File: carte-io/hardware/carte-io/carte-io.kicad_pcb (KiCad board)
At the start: 2 copper layers, 100 x 80 mm, 4 parts, among them J1 USB_C_Receptacle_USB2.0_14P, J2 Conn_01x02, U1 STM32U545VETx, U2 FT231XQ

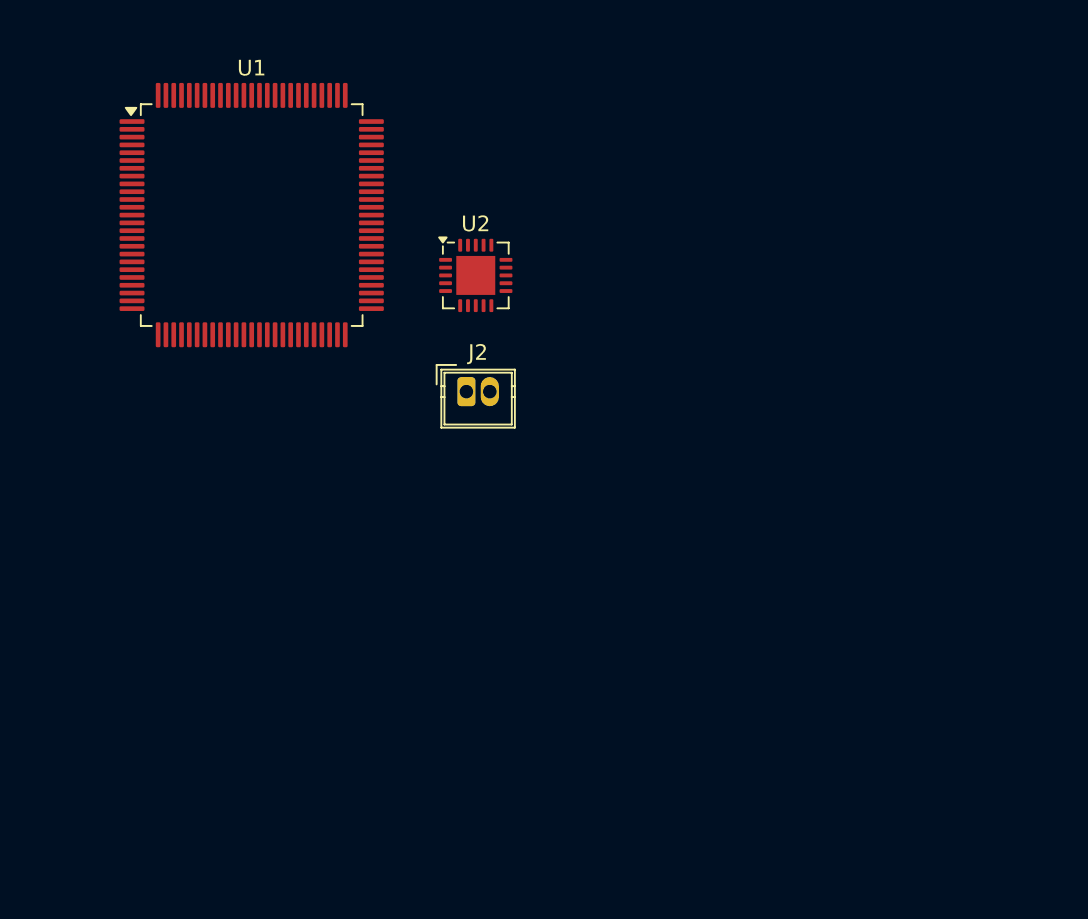
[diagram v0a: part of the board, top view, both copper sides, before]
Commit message: Selection de differents connecteurs
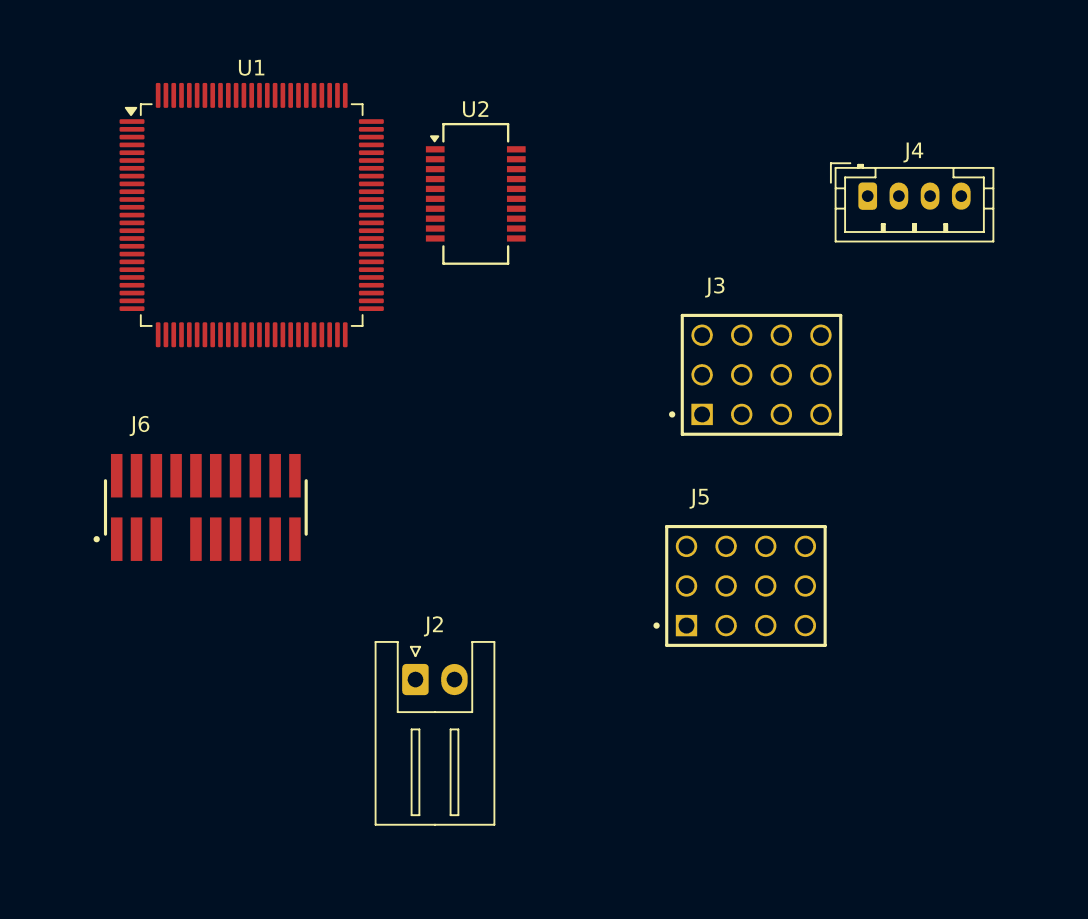
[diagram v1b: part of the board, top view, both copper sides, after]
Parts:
- added J3: TSW-104-07-G-T, TSW-104-07-G-T:SAMTEC_TSW-104-07-G-T, F.Cu at (177.2, 96.5)
- added J4: JST_PH_B4B, Connector_JST:JST_PH_B4B-PH-K_1x04_P2.00mm_Vertical, F.Cu at (184.0, 85.0)
- added J5: TSW-104-07-G-T, TSW-104-07-G-T:SAMTEC_TSW-104-07-G-T, F.Cu at (176.2, 110.0)
- added J6: FTSH-110-01-L-DV-007, FTSH-110-01-L-DV-007:SAMTEC_FTSH-110-01-L-DV-007, F.Cu at (141.6, 105.0)
- J2: value Conn_01x02 -> JST-XH_S2B-XH-A; footprint Connector_Wuerth:Wuerth_WR-WTB_64800211622_1x02_P1.50mm_Vertical -> Connector_JST:JST_XH_S2B-XH-A_1x02_P2.50mm_Horizontal
- U2: footprint Package_DFN_QFN:QFN-20-1EP_4x4mm_P0.5mm_EP2.5x2.5mm -> Package_SO:SSOP-20_3.9x8.7mm_P0.635mm
- moved J2 18.8 mm to (155.0, 116.0)
- moved U2 5.23 mm to (158.9, 84.9)
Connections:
- J1 pad A1: Net-(J1-GND-PadA1) -> GND
- J1 pad A12: Net-(J1-GND-PadA1) -> GND
- J1 pad A4: Net-(J1-VBUS-PadA4) -> unconnected-(J1-VBUS-PadA4)
- J1 pad A6: unconnected-(J1-D+-PadA6) -> Net-(U2-VCC)
- J1 pad A7: unconnected-(J1-D--PadA7) -> Net-(U2-VCC)
- J1 pad A9: Net-(J1-VBUS-PadA4) -> unconnected-(J1-VBUS-PadA4)_1
- J1 pad B1: Net-(J1-GND-PadA1) -> GND
- J1 pad B12: Net-(J1-GND-PadA1) -> GND
- J1 pad B4: Net-(J1-VBUS-PadA4) -> unconnected-(J1-VBUS-PadA4)_2
- J1 pad B6: unconnected-(J1-D+-PadB6) -> Net-(U2-USBDP)
- J1 pad B7: unconnected-(J1-D--PadB7) -> Net-(U2-USBDP)
- J1 pad B9: Net-(J1-VBUS-PadA4) -> unconnected-(J1-VBUS-PadA4)_3
- J1 pad S1: unconnected-(J1-SHIELD-PadS1) -> GND
- U2 pad 11: unconnected-(U2-~{RESET}-Pad11) -> Net-(U2-USBDP)
- U2 pad 12: unconnected-(U2-VCC-Pad12) -> Net-(U2-VCC)
- U2 pad 15: unconnected-(U2-CBUS0-Pad15) -> +3.3V
- U2 pad 16: unconnected-(U2-CBUS3-Pad16) -> GND
- U2 pad 3: unconnected-(U2-GND-Pad3) -> +3.3V
- U2 pad 6: unconnected-(U2-~{CTS}-Pad6) -> GND
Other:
- copper layers 2 -> 4

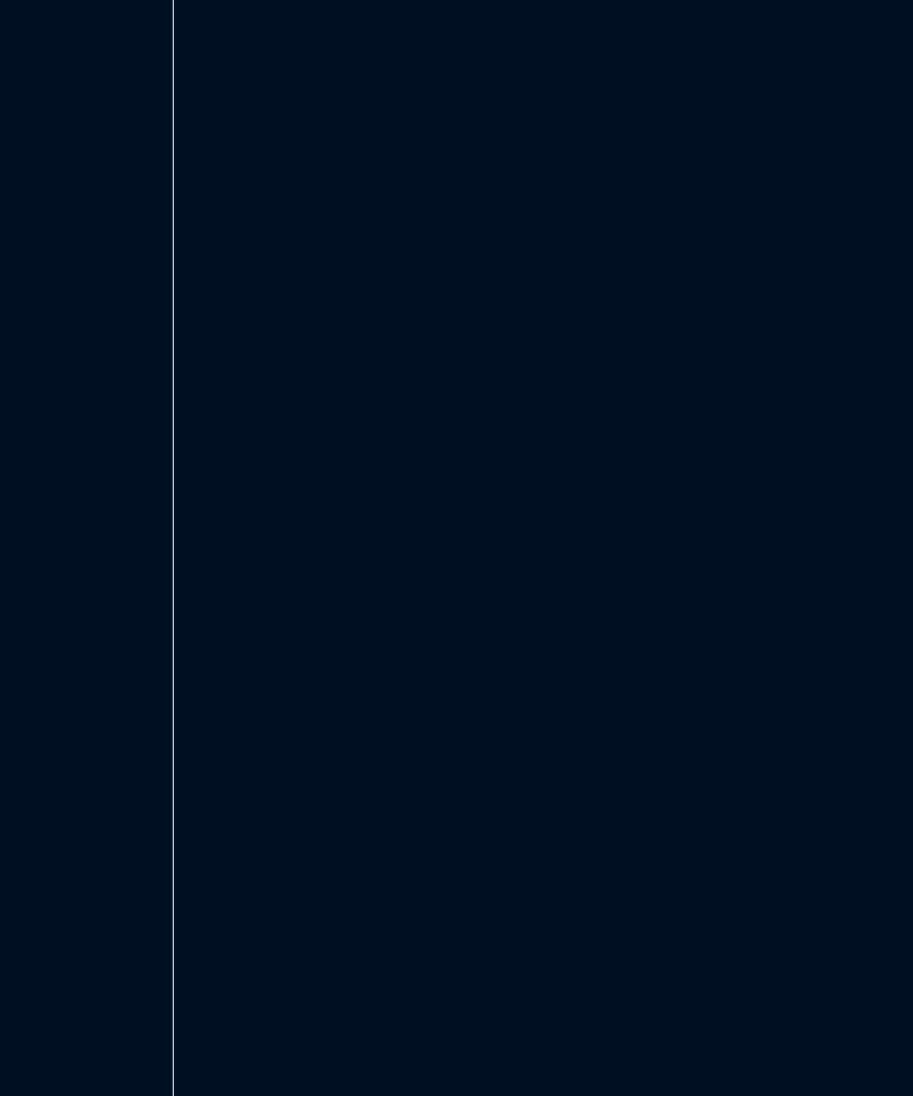
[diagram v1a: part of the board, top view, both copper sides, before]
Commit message: Evolution du schema de la carte IO + creation du projet STM32CubeIDE
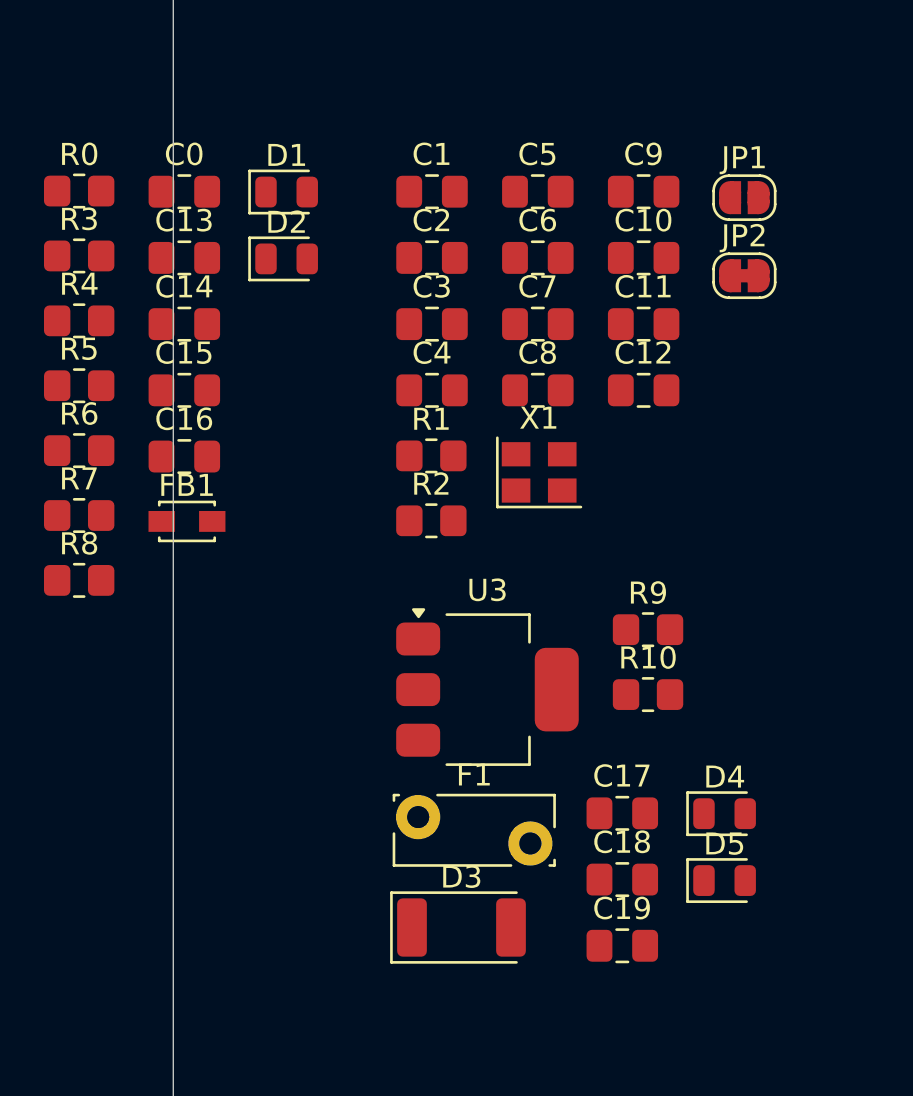
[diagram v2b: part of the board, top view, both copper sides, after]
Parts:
- added C0: 100nF, Capacitor_SMD:C_0805_2012Metric_Pad1.18x1.45mm_HandSolder, F.Cu at (100.5, 83.7)
- added C1: 10nF, Capacitor_SMD:C_0805_2012Metric_Pad1.18x1.45mm_HandSolder, F.Cu at (111.8, 83.7)
- added C10: 100nF, Capacitor_SMD:C_0805_2012Metric_Pad1.18x1.45mm_HandSolder, F.Cu at (121.4, 86.7)
- added C11: 100nF, Capacitor_SMD:C_0805_2012Metric_Pad1.18x1.45mm_HandSolder, F.Cu at (121.4, 89.7)
- added C12: 1µF, Capacitor_SMD:C_0805_2012Metric_Pad1.18x1.45mm_HandSolder, F.Cu at (121.4, 92.7)
- added C13: 10nF, Capacitor_SMD:C_0805_2012Metric_Pad1.18x1.45mm_HandSolder, F.Cu at (100.5, 86.7)
- added C14: 10nf, Capacitor_SMD:C_0805_2012Metric_Pad1.18x1.45mm_HandSolder, F.Cu at (100.5, 89.7)
- added C15: 47pF, Capacitor_SMD:C_0805_2012Metric_Pad1.18x1.45mm_HandSolder, F.Cu at (100.5, 92.7)
- added C16: 47pF, Capacitor_SMD:C_0805_2012Metric_Pad1.18x1.45mm_HandSolder, F.Cu at (100.5, 95.7)
- added C17: 100nF, Capacitor_SMD:C_0805_2012Metric_Pad1.18x1.45mm_HandSolder, F.Cu at (120.4, 111.9)
- added C18: 100nF, Capacitor_SMD:C_0805_2012Metric_Pad1.18x1.45mm_HandSolder, F.Cu at (120.4, 115.0)
- added C19: 100nF, Capacitor_SMD:C_0805_2012Metric_Pad1.18x1.45mm_HandSolder, F.Cu at (120.4, 118.0)
- added C2: 4.7nF, Capacitor_SMD:C_0805_2012Metric_Pad1.18x1.45mm_HandSolder, F.Cu at (111.8, 86.7)
- added C3: 100nF, Capacitor_SMD:C_0805_2012Metric_Pad1.18x1.45mm_HandSolder, F.Cu at (111.8, 89.7)
- added C4: 100nF, Capacitor_SMD:C_0805_2012Metric_Pad1.18x1.45mm_HandSolder, F.Cu at (111.8, 92.7)
- added C5: 100nF, Capacitor_SMD:C_0805_2012Metric_Pad1.18x1.45mm_HandSolder, F.Cu at (116.6, 83.7)
- added C6: 100nF, Capacitor_SMD:C_0805_2012Metric_Pad1.18x1.45mm_HandSolder, F.Cu at (116.6, 86.7)
- added C7: 100nF, Capacitor_SMD:C_0805_2012Metric_Pad1.18x1.45mm_HandSolder, F.Cu at (116.6, 89.7)
- added C8: 10µF, Capacitor_SMD:C_0805_2012Metric_Pad1.18x1.45mm_HandSolder, F.Cu at (116.6, 92.7)
- added C9: 1µF, Capacitor_SMD:C_0805_2012Metric_Pad1.18x1.45mm_HandSolder, F.Cu at (121.4, 83.7)
- added D1: LED, LED_SMD:LED_0805_2012Metric, F.Cu at (105.2, 83.7)
- added D2: LED, LED_SMD:LED_0805_2012Metric, F.Cu at (105.2, 86.7)
- added D3: D, Diode_SMD:D_2010_5025Metric, F.Cu at (113.1, 117.1)
- added D4: LED, LED_SMD:LED_0805_2012Metric, F.Cu at (125.1, 112.0)
- added D5: LED, LED_SMD:LED_0805_2012Metric, F.Cu at (125.1, 115.0)
- added F1: Polyfuse, Fuse:Fuse_Bourns_MF-RG300, F.Cu at (111.1, 112.1)
- added FB1: FerriteBead_Small, Inductor_SMD:L_Walsin_WLFM201209x, F.Cu at (100.6, 98.7)
- added JP1: SolderJumper_2_Open, Jumper:SolderJumper-2_P1.3mm_Open_RoundedPad1.0x1.5mm, F.Cu at (126.0, 84.0)
- added JP2: SolderJumper_2_Bridged, Jumper:SolderJumper-2_P1.3mm_Bridged_RoundedPad1.0x1.5mm, F.Cu at (126.0, 87.5)
- added R0: 100R, Resistor_SMD:R_0805_2012Metric_Pad1.20x1.40mm_HandSolder, F.Cu at (95.7, 83.7)
- added R1: 10K, Resistor_SMD:R_0805_2012Metric_Pad1.20x1.40mm_HandSolder, F.Cu at (111.7, 95.7)
- added R10: 100R, Resistor_SMD:R_0805_2012Metric_Pad1.20x1.40mm_HandSolder, F.Cu at (121.6, 106.5)
- added R2: 100R, Resistor_SMD:R_0805_2012Metric_Pad1.20x1.40mm_HandSolder, F.Cu at (111.7, 98.6)
- added R3: 5.1K, Resistor_SMD:R_0805_2012Metric_Pad1.20x1.40mm_HandSolder, F.Cu at (95.7, 86.6)
- added R4: 5.1K, Resistor_SMD:R_0805_2012Metric_Pad1.20x1.40mm_HandSolder, F.Cu at (95.7, 89.6)
- added R5: 100R, Resistor_SMD:R_0805_2012Metric_Pad1.20x1.40mm_HandSolder, F.Cu at (95.7, 92.5)
- added R6: 100R, Resistor_SMD:R_0805_2012Metric_Pad1.20x1.40mm_HandSolder, F.Cu at (95.7, 95.5)
- added R7: 27R, Resistor_SMD:R_0805_2012Metric_Pad1.20x1.40mm_HandSolder, F.Cu at (95.7, 98.4)
- added R8: 27R, Resistor_SMD:R_0805_2012Metric_Pad1.20x1.40mm_HandSolder, F.Cu at (95.7, 101.4)
- added R9: 100R, Resistor_SMD:R_0805_2012Metric_Pad1.20x1.40mm_HandSolder, F.Cu at (121.6, 103.6)
- added U3: LT1963AxST-3.3, Package_TO_SOT_SMD:SOT-223-3_TabPin2, F.Cu at (114.3, 106.3)
- added X1: ASE-16.000MHZ-LC-T, Oscillator:Oscillator_SMD_Abracon_ASE-4Pin_3.2x2.5mm, F.Cu at (116.6, 96.4)
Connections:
- J1 pad A4: unconnected-(J1-VBUS-PadA4) -> VBUS
- J1 pad A5: unconnected-(J1-CC1-PadA5) -> Net-(J1-CC1)
- J1 pad A6: Net-(U2-VCC) -> Net-(C16-Pad1)
- J1 pad A7: Net-(U2-VCC) -> Net-(C16-Pad1)
- J1 pad A9: unconnected-(J1-VBUS-PadA4)_1 -> VBUS
- J1 pad B4: unconnected-(J1-VBUS-PadA4)_2 -> VBUS
- J1 pad B5: unconnected-(J1-CC2-PadB5) -> Net-(J1-CC2)
- J1 pad B6: Net-(U2-USBDP) -> Net-(C15-Pad1)
- J1 pad B7: Net-(U2-USBDP) -> Net-(C15-Pad1)
- J1 pad B9: unconnected-(J1-VBUS-PadA4)_3 -> VBUS
- J2 pad 1: unconnected-(J2-Pin_1-Pad1) -> GND
- J2 pad 2: unconnected-(J2-Pin_2-Pad2) -> Net-(J2-Pin_2)
- U1 pad 10: Net-(U1-VSS-Pad10) -> GND
- U1 pad 100: unconnected-(U1-VDD-Pad100) -> +3.3V
- U1 pad 11: unconnected-(U1-VDD-Pad11) -> +3.3V
- U1 pad 12: unconnected-(U1-PH0-Pad12) -> /CPU/CLK_IN_16Mhz
- U1 pad 14: unconnected-(U1-NRST-Pad14) -> /CPU/NRST
- U1 pad 15: unconnected-(U1-PC0-Pad15) -> /CPU/LPUART1_RX
- U1 pad 16: unconnected-(U1-PC1-Pad16) -> /CPU/COM_EXT_TX
- U1 pad 17: unconnected-(U1-PC2-Pad17) -> /CPU/SPI2_MISO
- U1 pad 18: unconnected-(U1-PC3-Pad18) -> /CPU/SPI2_MOSI
- U1 pad 19: unconnected-(U1-VSSA-Pad19) -> GND
- U1 pad 2: unconnected-(U1-PE3-Pad2) -> /CPU/ENCODER_3_PHA
- U1 pad 20: unconnected-(U1-VREF--Pad20) -> GND
- U1 pad 21: unconnected-(U1-VREF+-Pad21) -> +3.3V
- U1 pad 22: unconnected-(U1-VDDA-Pad22) -> VDDA
- U1 pad 23: unconnected-(U1-PA0-Pad23) -> /CPU/MOT_PWM1
- U1 pad 24: unconnected-(U1-PA1-Pad24) -> /CPU/MOT_PWM2
- U1 pad 25: unconnected-(U1-PA2-Pad25) -> /CPU/MOT_PWM3
- U1 pad 26: unconnected-(U1-PA3-Pad26) -> /CPU/MOT_PWM4
- U1 pad 27: Net-(U1-VSS-Pad10) -> GND
- U1 pad 28: unconnected-(U1-VDD-Pad28) -> +3.3V
- U1 pad 29: unconnected-(U1-PA4-Pad29) -> /CPU/US_PWM
- U1 pad 3: unconnected-(U1-PE4-Pad3) -> /CPU/ENCODER_3_PHB
- U1 pad 30: unconnected-(U1-PA5-Pad30) -> /CPU/PWR_CSLEEP
- U1 pad 31: unconnected-(U1-PA6-Pad31) -> /CPU/SPI_MISO
- U1 pad 32: unconnected-(U1-PA7-Pad32) -> /CPU/I2C3_SCL
- U1 pad 33: unconnected-(U1-PC4-Pad33) -> /CPU/COM_GPS_TX
- U1 pad 34: unconnected-(U1-PC5-Pad34) -> /CPU/COM_GPS_RX
- U1 pad 35: unconnected-(U1-PB0-Pad35) -> /CPU/SERVO_PWM2N
- U1 pad 37: unconnected-(U1-PB2-Pad37) -> /CPU/ADC_VBAT
- U1 pad 40: unconnected-(U1-PE9-Pad40) -> /CPU/ENCODER_1_PHA
- U1 pad 42: unconnected-(U1-PE11-Pad42) -> /CPU/ENCODER_1_PHB
- U1 pad 44: unconnected-(U1-PE13-Pad44) -> /CPU/SPI_SCK
- U1 pad 46: unconnected-(U1-PE15-Pad46) -> /CPU/SPI_MOSI
- U1 pad 47: unconnected-(U1-PB10-Pad47) -> /CPU/ENCODER_2_PHB
- U1 pad 48: unconnected-(U1-VCAP-Pad48) -> Net-(U1-VCAP)
- U1 pad 49: Net-(U1-VSS-Pad10) -> GND
- U1 pad 50: unconnected-(U1-VDD-Pad50) -> +3.3V
- U1 pad 52: unconnected-(U1-PB13-Pad52) -> /CPU/SPI2_SCK
- U1 pad 53: unconnected-(U1-PB14-Pad53) -> /CPU/GEN_PWM1
- U1 pad 54: unconnected-(U1-PB15-Pad54) -> /CPU/GEN_PWM2
- U1 pad 59: unconnected-(U1-PD12-Pad59) -> /CPU/ENCODER_4_PHA
- U1 pad 6: unconnected-(U1-VBAT-Pad6) -> +3.3V
- U1 pad 60: unconnected-(U1-PD13-Pad60) -> /CPU/ENCODER_4_PHB
- U1 pad 63: unconnected-(U1-PC6-Pad63) -> /CPU/SERVO_PWM1
- U1 pad 65: unconnected-(U1-PC8-Pad65) -> /CPU/SERVO_PWM3
- U1 pad 66: unconnected-(U1-PC9-Pad66) -> /CPU/SERVO_PWM4
- U1 pad 68: unconnected-(U1-PA9-Pad68) -> /CPU/COM_USB_TX
- U1 pad 69: unconnected-(U1-PA10-Pad69) -> /CPU/COM_USB_RX
- U1 pad 70: unconnected-(U1-PA11-Pad70) -> /CPU/FDCAN1_RX
- U1 pad 71: unconnected-(U1-PA12-Pad71) -> /CPU/FDCAN1_TX
- U1 pad 72: unconnected-(U1-PA13-Pad72) -> /CPU/JTMS-SWDIO
- U1 pad 73: unconnected-(U1-VDDUSB-Pad73) -> +3.3V
- U1 pad 74: Net-(U1-VSS-Pad10) -> GND
- U1 pad 75: unconnected-(U1-VDD-Pad75) -> +3.3V
- U1 pad 76: unconnected-(U1-PA14-Pad76) -> /CPU/JTCK-SWCLK
- U1 pad 77: unconnected-(U1-PA15-Pad77) -> /CPU/ENCODER_2_PHA
- U1 pad 78: unconnected-(U1-PC10-Pad78) -> /CPU/COM_LIDAR1_TX
- U1 pad 79: unconnected-(U1-PC11-Pad79) -> /CPU/COM_LIDAR1_RX
- U1 pad 80: unconnected-(U1-PC12-Pad80) -> /CPU/COM_LIDAR2_TX
- U1 pad 83: unconnected-(U1-PD2-Pad83) -> /CPU/COM_LIDAR2_RX
- U1 pad 89: unconnected-(U1-PB3-Pad89) -> /CPU/JTDO-SWO
- U1 pad 90: unconnected-(U1-PB4-Pad90) -> /CPU/I2C_SDA_EXT
- U1 pad 92: unconnected-(U1-PB6-Pad92) -> /CPU/I2C_SCL_INT
- U1 pad 93: unconnected-(U1-PB7-Pad93) -> /CPU/I2C_SDA_EXT
- U1 pad 94: unconnected-(U1-PH3-Pad94) -> Net-(U1-PH3)
- U1 pad 99: Net-(U1-VSS-Pad10) -> GND
- U2 pad 10: unconnected-(U2-CBUS2-Pad10) -> Net-(D2-K)
- U2 pad 12: Net-(U2-VCC) -> Net-(U2-USBDM)
- U2 pad 13: unconnected-(U2-3V3OUT-Pad13) -> Net-(U2-3V3OUT)
- U2 pad 14: unconnected-(U2-~{RESET}-Pad14) -> Net-(U2-3V3OUT)
- U2 pad 15: +3.3V -> Net-(U2-VCC)
- U2 pad 17: unconnected-(U2-CBUS1-Pad17) -> Net-(D1-K)
- U2 pad 20: unconnected-(U2-TXD-Pad20) -> /IO/USB_UART_TX
- U2 pad 3: +3.3V -> Net-(U2-3V3OUT)
- U2 pad 4: unconnected-(U2-RXD-Pad4) -> /IO/USB_UART_RX
